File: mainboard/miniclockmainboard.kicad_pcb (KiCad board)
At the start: 2 copper layers, 38 x 40 mm, 15 parts, among them P1 CONN_9, P2 CONN_6, P3 CONN_7, SW1 SW_PUSH, SW2 SW_PUSH, U1 LD1117, U2 DS3231M, U3 LPC812M101JD20

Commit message: Add some silkscreen captions to the rear of the main board.
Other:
- board text added: "Mini Clock Main Board v0.1"
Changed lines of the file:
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@@
     (area 107.949999 102.949999 146.050001 143.050001)
     (thickness 1.6)
-    (drawings 14)
+    (drawings 15)
     (tracks 177)
     (zones 0)
@@
   (page A4)
   (layers
-    (0 F.Cu signal hide)
-    (31 B.Cu signal hide)
+    (0 F.Cu signal)
+    (31 B.Cu signal)
     (32 B.Adhes user)
     (33 F.Adhes user)
@@
     )
   )
+  (gr_text "Mini Clock\nMain Board\nv0.1" (at 134.5 136.5) (layer B.SilkS)
+    (effects (font (size 1.5 1.5) (thickness 0.3)) (justify mirror))
+  )
   (target plus (at 110 105) (size 5) (width 0.1) (layer Edge.Cuts))

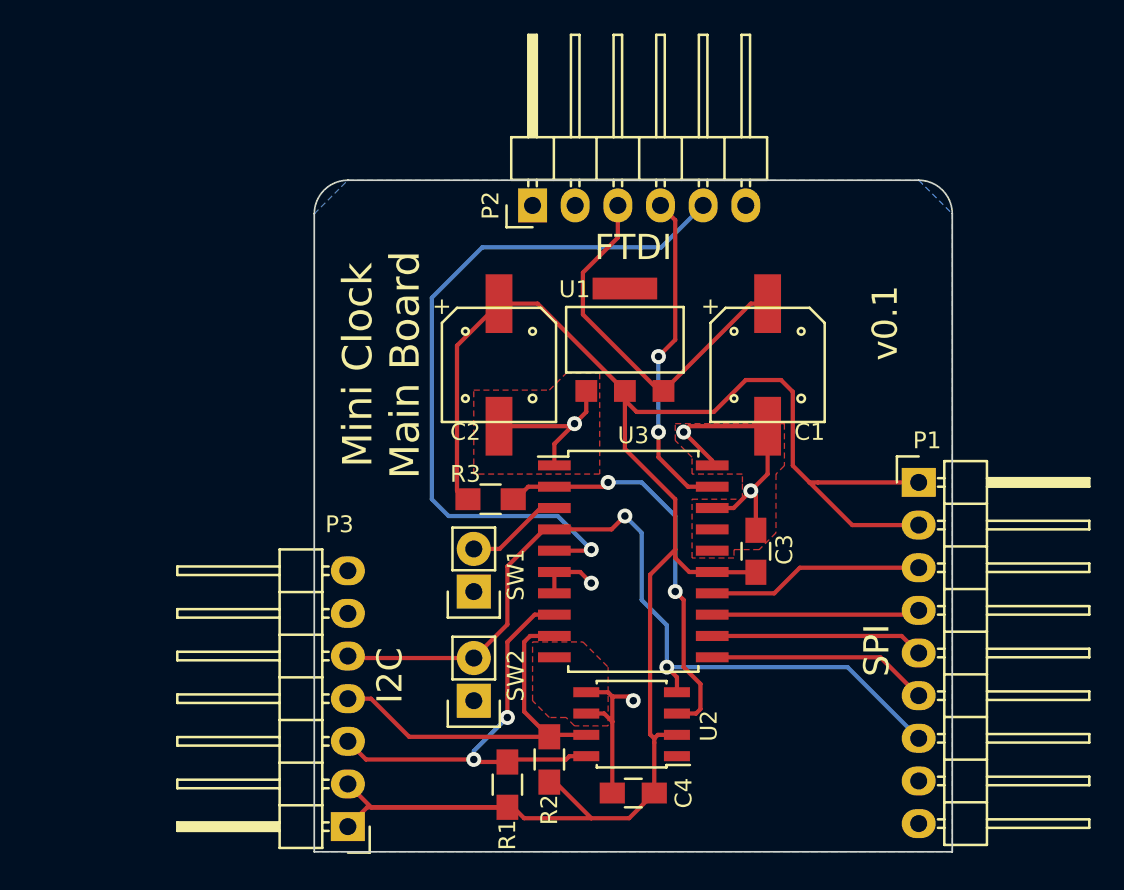
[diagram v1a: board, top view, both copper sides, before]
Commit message: Shrink the main board width.
Previous version was slightly too wide for the first prototype's
enclosure. The new size is much smaller than the available space in the
enclosure.
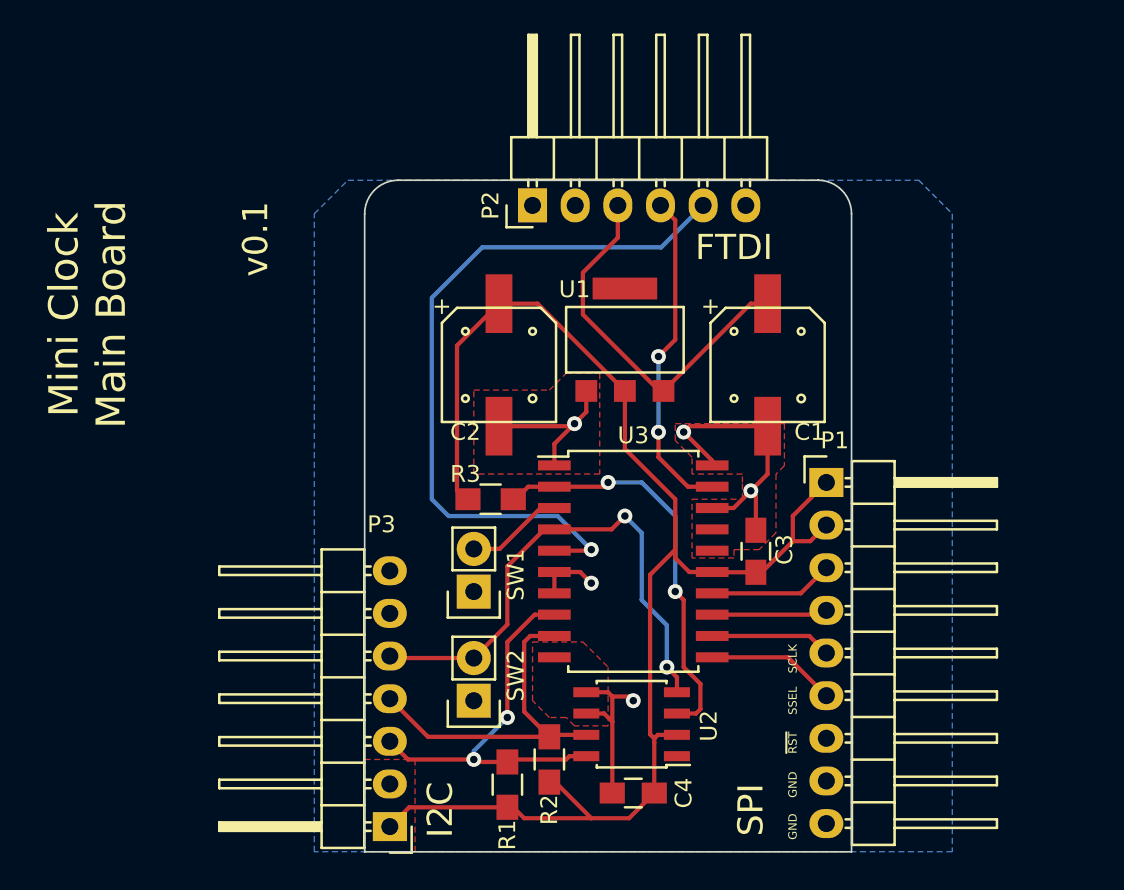
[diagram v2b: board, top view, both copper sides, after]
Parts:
- moved P1 5.50 mm to (138.5, 121.0)
- moved P3 2.50 mm to (112.5, 141.5)
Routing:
- net VCC: track 121.1 -> 87.0 mm
- net /~RST: track 50.6 -> 31.4 mm
- net /SCLK: track 13.1 -> 7.22 mm
- net /MOSI: track 12.9 -> 7.43 mm
- net /SSEL: track 13.2 -> 7.75 mm
- net /MISO: track 12.4 -> 6.91 mm
- net /SDA: track 23.4 -> 20.9 mm
- net /SCL: track 26.5 -> 24.0 mm
- added copper zone on F.Cu, net VCC
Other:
- board size 38 x 40 mm -> 29 x 40 mm
- board text added: "GND"
- board text added: "SCLK"
- board text added: "SSEL"
- board text added: "~RST"

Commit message: Fix up the pad positions on the polarized caps.
The pads were incorrectly spaced before since the space between the pad
edges was confused with the space between the centers.
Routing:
- net /+5V: track 22.4 -> 21.7 mm
